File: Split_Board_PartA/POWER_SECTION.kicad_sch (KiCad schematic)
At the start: 19 parts, among them J6 Conn_01x10, U36 LM1117-3.3

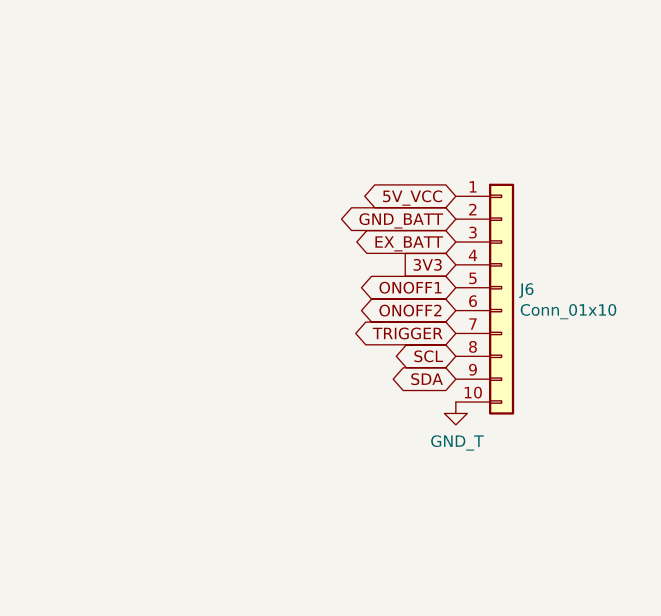
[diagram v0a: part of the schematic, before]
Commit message: added a led pins on part A connecttor, added adapter board  and led connector on adapter board, added pdf of design files of voidron part b is upto date part A final is remaining. Adapter board is also ok
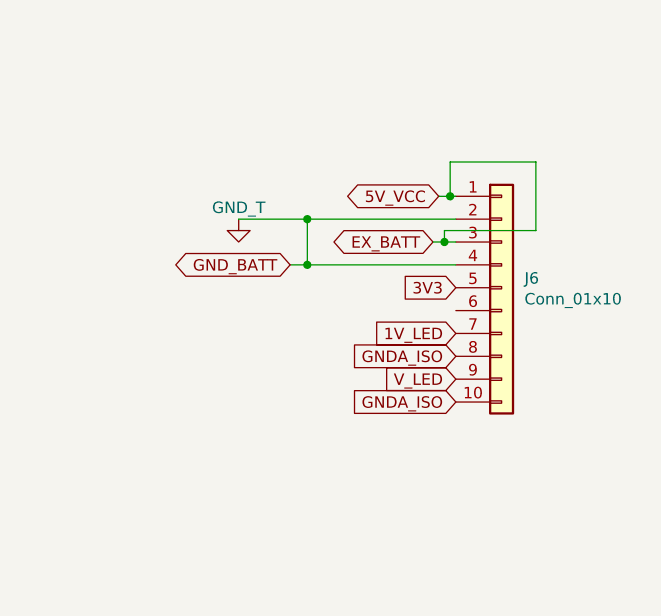
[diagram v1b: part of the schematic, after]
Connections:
- net EX_BATT is gone; now on net 5V_VCC: J6.3 (Pin_3)
- net GND_BATT is gone; now on net GND: J6.2 (Pin_2)
- net ONOFF1 is gone; now on net 3V3: J6.5 (Pin_5)
- net SCL is gone; now on net GNDA_ISO: J6.8 (Pin_8)
- net 3V3: no longer J6.4 (Pin_4)
- net GND: now also J6.4 (Pin_4); no longer J6.10 (Pin_10)
- net GNDA_ISO: now also J6.10 (Pin_10)
- net ONOFF2: no longer names the net of J6.6 (Pin_6)
- net SDA renamed V_LED
- net TRIGGER renamed 1V_LED
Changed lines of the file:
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@@
   (junction (at 60.325 131.445) (diameter 0) (color 0 0 0 0)
   )
+  (junction (at 224.155 53.975) (diameter 0) (color 0 0 0 0)
+  )
+  (junction (at 239.395 56.515) (diameter 0) (color 0 0 0 0)
+  )
+  (junction (at 224.155 59.055) (diameter 0) (color 0 0 0 0)
+  )
   (junction (at 48.895 61.595) (diameter 0) (color 0 0 0 0)
   )
@@
   (junction (at 93.345 59.055) (diameter 0) (color 0 0 0 0)
   )
+  (junction (at 240.03 51.435) (diameter 0) (color 0 0 0 0)
+  )
   (junction (at 93.345 66.675) (diameter 0) (color 0 0 0 0)
   )
@@
     (stroke (width 0) (type default))
   )
+  (wire (pts (xy 224.155 53.975) (xy 224.155 59.055))
+    (stroke (width 0) (type default))
+  )
+  (wire (pts (xy 238.76 51.435) (xy 240.03 51.435))
+    (stroke (width 0) (type default))
+  )
   (wire (pts (xy 104.14 66.675) (xy 127 66.675))
     (stroke (width 0) (type default))
   )
+  (wire (pts (xy 239.395 55.245) (xy 249.555 55.245))
+    (stroke (width 0) (type default))
+  )
   (wire (pts (xy 48.895 62.865) (xy 48.895 61.595))
     (stroke (width 0) (type default))
@@
     (stroke (width 0) (type default))
   )
+  (wire (pts (xy 239.395 56.515) (xy 240.665 56.515))
+    (stroke (width 0) (type default))
+  )
   (wire (pts (xy 86.36 66.675) (xy 93.345 66.675))
     (stroke (width 0) (type default))
@@
     (stroke (width 0) (type default))
   )
+  (wire (pts (xy 224.155 53.975) (xy 240.665 53.975))
+    (stroke (width 0) (type default))
+  )
   (wire (pts (xy 42.545 70.485) (xy 42.545 71.755))
     (stroke (width 0) (type default))
   )
+  (wire (pts (xy 222.25 59.055) (xy 224.155 59.055))
+    (stroke (width 0) (type default))
+  )
   (wire (pts (xy 104.14 57.15) (xy 104.14 59.055))
     (stroke (width 0) (type default))
@@
     (stroke (width 0) (type default))
   )
+  (wire (pts (xy 249.555 47.625) (xy 249.555 55.245))
+    (stroke (width 0) (type default))
+  )
+  (wire (pts (xy 240.03 47.625) (xy 249.555 47.625))
+    (stroke (width 0) (type default))
+  )
   (wire (pts (xy 42.545 61.595) (xy 48.895 61.595))
     (stroke (width 0) (type default))
@@
     (stroke (width 0) (type default))
   )
+  (wire (pts (xy 238.125 56.515) (xy 239.395 56.515))
+    (stroke (width 0) (type default))
+  )
+  (wire (pts (xy 239.395 55.245) (xy 239.395 56.515))
+    (stroke (width 0) (type default))
+  )
   (wire (pts (xy 42.545 62.865) (xy 42.545 61.595))
     (stroke (width 0) (type default))
@@
     (stroke (width 0) (type default))
   )
+  (wire (pts (xy 240.03 47.625) (xy 240.03 51.435))
+    (stroke (width 0) (type default))
+  )
+  (wire (pts (xy 240.03 51.435) (xy 240.665 51.435))
+    (stroke (width 0) (type default))
+  )
   (wire (pts (xy 48.895 71.755) (xy 55.88 71.755))
     (stroke (width 0) (type default))
   )
+  (wire (pts (xy 216.535 53.975) (xy 224.155 53.975))
+    (stroke (width 0) (type default))
+  )
   (wire (pts (xy 104.14 76.2) (xy 104.14 74.295))
     (stroke (width 0) (type default))
@@
   )
   (wire (pts (xy 78.359 131.445) (xy 83.185 131.445))
+    (stroke (width 0) (type default))
+  )
+  (wire (pts (xy 224.155 59.055) (xy 240.665 59.055))
     (stroke (width 0) (type default))
   )
@@
   (text "VOLTAGE ISOLATION SECTION " (at 25.4 18.415 0)
     (effects (font (size 2.9972 2.9972) (thickness 0.5994) bold) (justify left bottom))
+  )
+  (global_label "1V_LED" (shape input) (at 240.665 66.675 180)
+    (effects (font (size 1.27 1.27)) (justify right))
+    (property "Intersheetrefs" "${INTERSHEET_REFS}" (at 240.665 66.675 0)
+      (effects (font (size 1.27 1.27)) hide)
+    )
   )
   (global_label "5V_VCC" (shape input) (at 48.895 58.801 90) (fields_autoplaced)
@@
     )
   )
-  (global_label "3V3" (shape input) (at 240.665 59.055 180) (fields_autoplaced)
-    (effects (font (size 1.27 1.27)) (justify right))
-    (property "Intersheetrefs" "${INTERSHEET_REFS}" (at 234.9058 59.055 0)
+  (global_label "3V3" (shape input) (at 240.665 61.595 180) (fields_autoplaced)
+    (effects (font (size 1.27 1.27)) (justify right))
+    (property "Intersheetrefs" "${INTERSHEET_REFS}" (at 234.9058 61.595 0)
+      (effects (font (size 1.27 1.27)) (justify right) hide)
+    )
+  )
+  (global_label "GNDA_ISO" (shape input) (at 240.665 74.295 180) (fields_autoplaced)
+    (effects (font (size 1.27 1.27)) (justify right))
+    (property "Intersheetrefs" "${INTERSHEET_REFS}" (at 228.6877 74.295 0)
       (effects (font (size 1.27 1.27)) (justify right) hide)
     )
@@
     )
   )
-  (global_label "SDA" (shape bidirectional) (at 240.665 71.755 180) (fields_autoplaced)
-    (effects (font (size 1.27 1.27)) (justify right))
-    (property "Intersheetrefs" "${INTERSHEET_REFS}" (at 233.8928 71.755 0)
-      (effects (font (size 1.27 1.27)) (justify right) hide)
-    )
-  )
-  (global_label "EX_BATT" (shape bidirectional) (at 240.665 56.515 180) (fields_autoplaced)
-    (effects (font (size 1.27 1.27)) (justify right))
-    (property "Intersheetrefs" "${INTERSHEET_REFS}" (at 229.841 56.515 0)
-      (effects (font (size 1.27 1.27)) (justify right) hide)
-    )
-  )
-  (global_label "ONOFF1" (shape bidirectional) (at 240.665 61.595 180) (fields_autoplaced)
-    (effects (font (size 1.27 1.27)) (justify right))
-    (property "Intersheetrefs" "${INTERSHEET_REFS}" (at 230.0827 61.595 0)
-      (effects (font (size 1.27 1.27)) (justify right) hide)
-    )
-  )
-  (global_label "SCL" (shape bidirectional) (at 240.665 69.215 180) (fields_autoplaced)
-    (effects (font (size 1.27 1.27)) (justify right))
-    (property "Intersheetrefs" "${INTERSHEET_REFS}" (at 233.9533 69.215 0)
-      (effects (font (size 1.27 1.27)) (justify right) hide)
-    )
-  )
-  (global_label "GND_BATT" (shape bidirectional) (at 240.665 53.975 180) (fields_autoplaced)
-    (effects (font (size 1.27 1.27)) (justify right))
-    (property "Intersheetrefs" "${INTERSHEET_REFS}" (at 228.329 53.975 0)
+  (global_label "EX_BATT" (shape bidirectional) (at 238.125 56.515 180) (fields_autoplaced)
+    (effects (font (size 1.27 1.27)) (justify right))
+    (property "Intersheetrefs" "${INTERSHEET_REFS}" (at 227.301 56.515 0)
+      (effects (font (size 1.27 1.27)) (justify right) hide)
+    )
+  )
+  (global_label "GND_BATT" (shape bidirectional) (at 222.25 59.055 180) (fields_autoplaced)
+    (effects (font (size 1.27 1.27)) (justify right))
+    (property "Intersheetrefs" "${INTERSHEET_REFS}" (at 209.914 59.055 0)
       (effects (font (size 1.27 1.27)) (justify right) hide)
     )
@@
     (effects (font (size 1.27 1.27)) (justify right))
     (property "Intersheetrefs" "${INTERSHEET_REFS}" (at 104.14 87.5231 90)
-      (effects (font (size 1.27 1.27)) (justify right) hide)
-    )
-  )
-  (global_label "ONOFF2" (shape bidirectional) (at 240.665 64.135 180) (fields_autoplaced)
-    (effects (font (size 1.27 1.27)) (justify right))
-    (property "Intersheetrefs" "${INTERSHEET_REFS}" (at 230.0827 64.135 0)
-      (effects (font (size 1.27 1.27)) (justify right) hide)
-    )
-  )
-  (global_label "TRIGGER" (shape bidirectional) (at 240.665 66.675 180) (fields_autoplaced)
-    (effects (font (size 1.27 1.27)) (justify right))
-    (property "Intersheetrefs" "${INTERSHEET_REFS}" (at 229.6595 66.675 0)
       (effects (font (size 1.27 1.27)) (justify right) hide)
     )
@@
     )
   )
-  (global_label "5V_VCC" (shape bidirectional) (at 240.665 51.435 180) (fields_autoplaced)
-    (effects (font (size 1.27 1.27)) (justify right))
-    (property "Intersheetrefs" "${INTERSHEET_REFS}" (at 230.5666 51.435 0)
+  (global_label "V_LED" (shape input) (at 240.665 71.755 180)
+    (effects (font (size 1.27 1.27)) (justify right))
+    (property "Intersheetrefs" "${INTERSHEET_REFS}" (at 240.665 71.755 0)
+      (effects (font (size 1.27 1.27)) hide)
+    )
+  )
+  (global_label "GNDA_ISO" (shape input) (at 240.665 69.215 180) (fields_autoplaced)
+    (effects (font (size 1.27 1.27)) (justify right))
+    (property "Intersheetrefs" "${INTERSHEET_REFS}" (at 228.6877 69.215 0)
+      (effects (font (size 1.27 1.27)) (justify right) hide)
+    )
+  )
+  (global_label "5V_VCC" (shape bidirectional) (at 238.76 51.435 180) (fields_autoplaced)
+    (effects (font (size 1.27 1.27)) (justify right))
+    (property "Intersheetrefs" "${INTERSHEET_REFS}" (at 228.6616 51.435 0)
       (effects (font (size 1.27 1.27)) (justify right) hide)
     )
@@
   (symbol (lib_id "Connector_Generic:Conn_01x10") (at 245.745 61.595 0) (unit 1)
     (in_bom yes) (on_board yes) (dnp no)
-    (property "Reference" "J6" (at 247.777 61.7982 0)
-      (effects (font (size 1.27 1.27)) (justify left))
-    )
-    (property "Value" "Conn_01x10" (at 247.777 64.1096 0)
+    (property "Reference" "J6" (at 248.285 60.5536 0)
+      (effects (font (size 1.27 1.27)) (justify left))
+    )
+    (property "Value" "Conn_01x10" (at 248.285 62.865 0)
       (effects (font (size 1.27 1.27)) (justify left))
     )
@@
     )
   )
-  (symbol (lib_id "ohm3000Board-rescue:GND_T") (at 240.665 74.295 0) (unit 1)
-    (in_bom yes) (on_board yes) (dnp no)
-    (property "Reference" "#PWR0123" (at 240.665 80.645 0)
-      (effects (font (size 1.27 1.27)) hide)
-    )
-    (property "Value" "GND_T" (at 240.792 78.6892 0)
+  (symbol (lib_id "ohm3000Board-rescue:GND_T") (at 216.535 53.975 0) (unit 1)
+    (in_bom yes) (on_board yes) (dnp no)
+    (property "Reference" "#PWR0123" (at 216.535 60.325 0)
+      (effects (font (size 1.27 1.27)) hide)
+    )
+    (property "Value" "GND_T" (at 216.535 52.705 0)
       (effects (font (size 1.27 1.27)))
     )
-    (property "Footprint" "" (at 240.665 74.295 0)
-      (effects (font (size 1.27 1.27)) hide)
-    )
-    (property "Datasheet" "" (at 240.665 74.295 0)
-      (effects (font (size 1.27 1.27)) hide)
-    )
+    (property "Footprint" "" (at 216.535 53.975 0)
+      (effects (font (size 1.27 1.27)) hide)
+    )
+    (property "Datasheet" "" (at 216.535 53.975 0)
+      (effects (font (size 1.27 1.27)) hide)
+    )

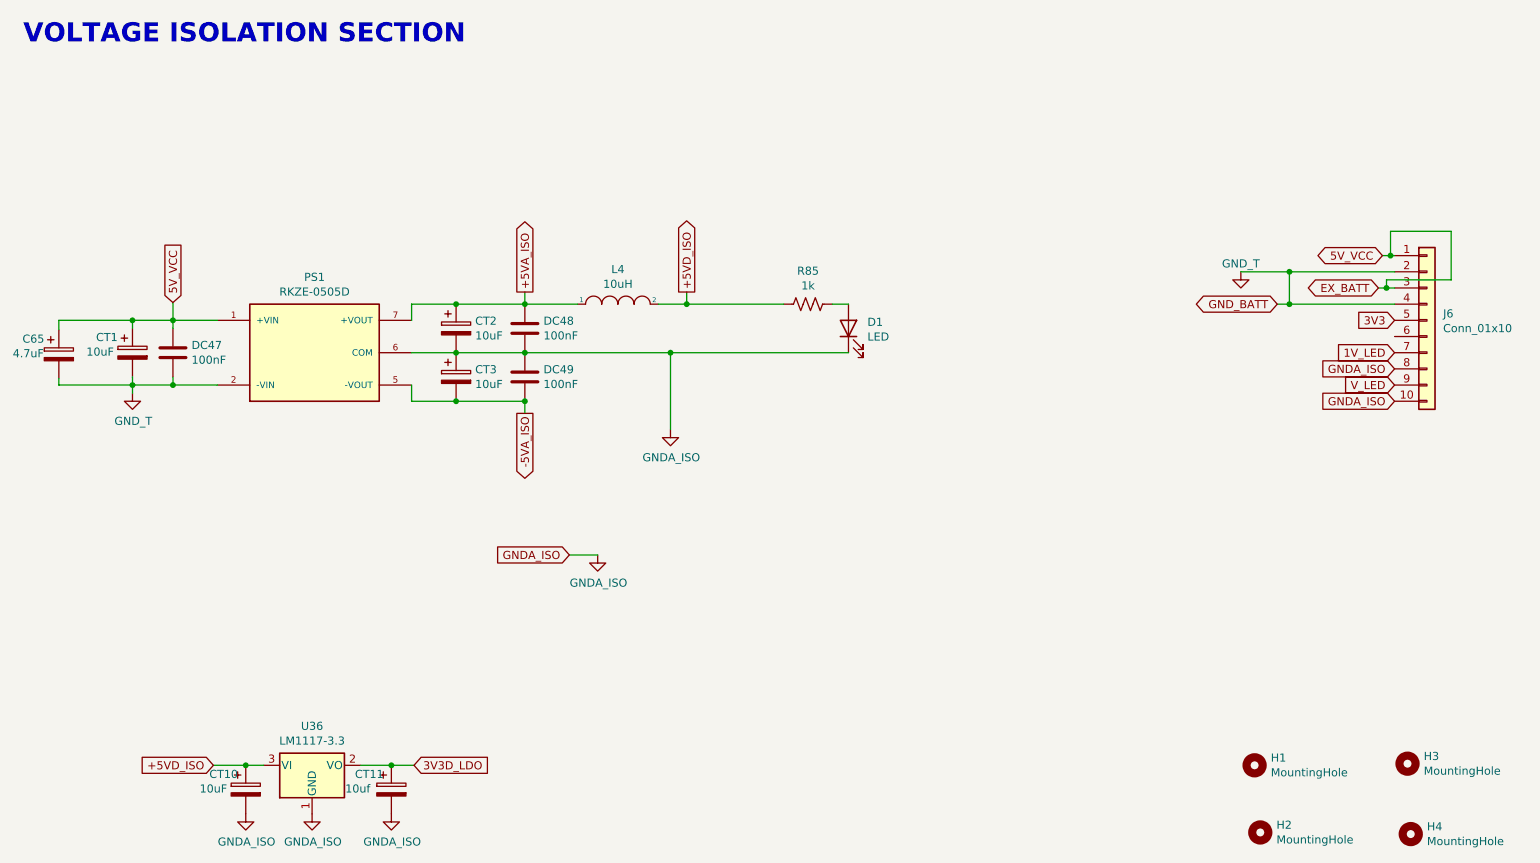
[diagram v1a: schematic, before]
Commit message: changed the part A power section, added the ground GNDD_ISO
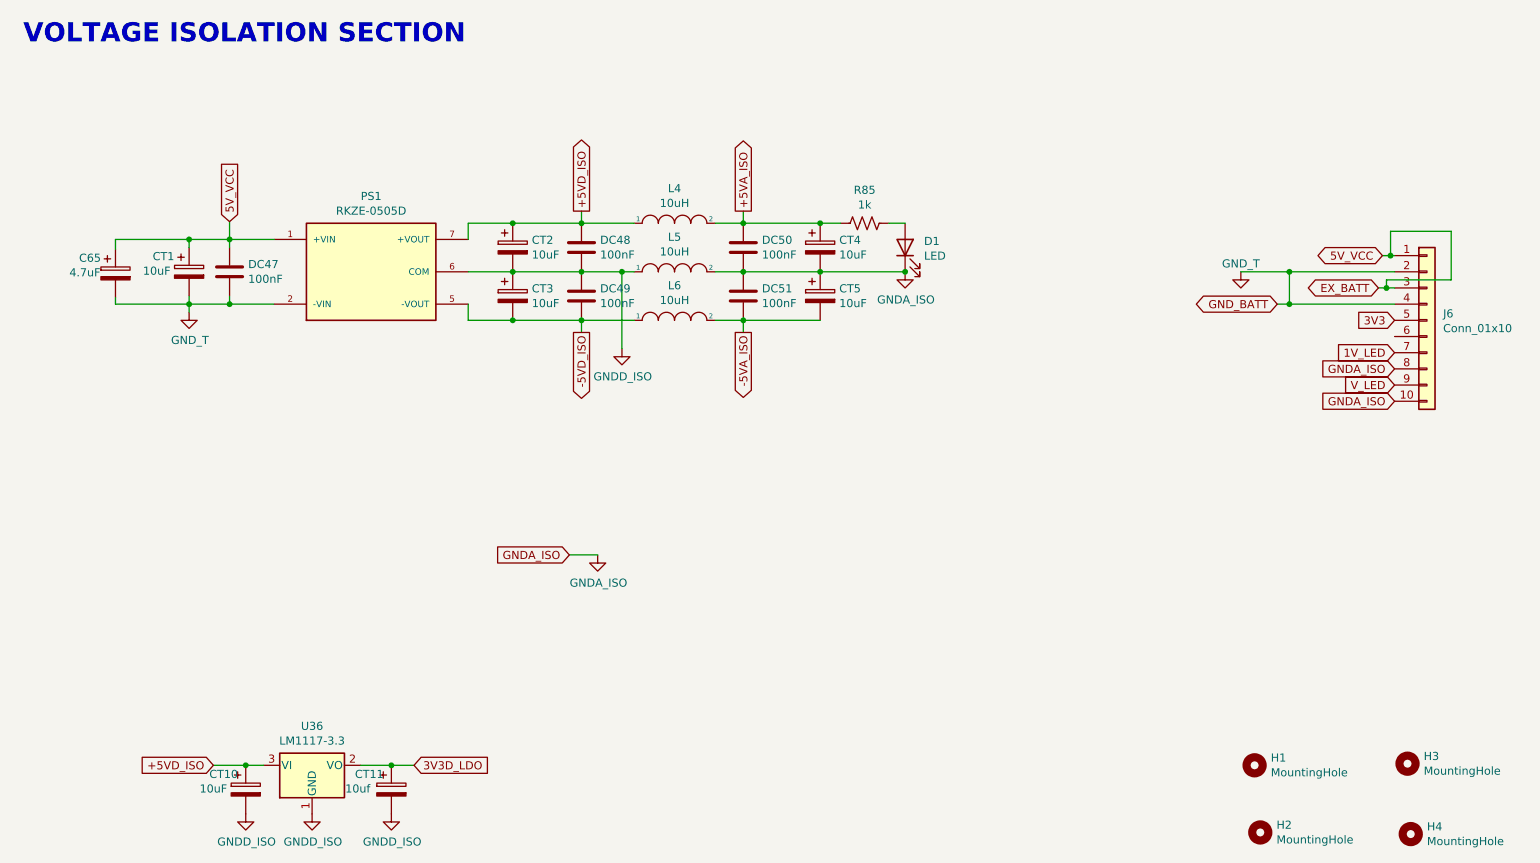
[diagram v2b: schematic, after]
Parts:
- added CT4, CT5: 10uF, Capacitor_Tantalum_SMD:CP_EIA-3216-18_Kemet-A, symbol ohm3000Board-rescue:CP-Device
- added DC50, DC51: 100nF, Capacitor_SMD:C_1206_3216Metric, symbol Device:C
- added L5, L6: 10uH, Inductor_SMD:L_1206_3216Metric, symbol pspice:INDUCTOR
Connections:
- net +5VA_ISO: now also L4.2, R85.2, CT4.1, DC50.1; no longer CT2.1, DC48.1, L4.1, PS1.7 (+VOUT)
- net +5VD_ISO: now also CT2.1, DC48.1, L4.1, PS1.7 (+VOUT); no longer L4.2, R85.2
- net -5VA_ISO: now also CT5.2, DC51.2, L6.2; no longer CT3.2, DC49.2, PS1.5 (-VOUT)
- net GNDA_ISO: now also CT4.2, CT5.1, DC50.2, DC51.1, L5.2; no longer CT2.2, CT3.1, DC48.2, DC49.1, PS1.6 (COM)
- net GNDD_ISO: now also CT2.2, CT3.1, DC48.2, DC49.1, PS1.6 (COM), L5.1
- new net -5VD_ISO: CT3.2, DC49.2, L6.1, PS1.5 (-VOUT)
